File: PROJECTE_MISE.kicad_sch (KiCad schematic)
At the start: 37 parts, among them IC1 MSP430FR2355TPT, J1 conn_DFrobot, J2 ESP01_WiFi_mod, J3 Conn_TX_TP, J4 conn_ACLK_{TP}, J5 conn_SMCLK_{TP}, J6 Conn_RX_TP, J7 conn_SBW, SW1 ~{RST_{MSP}}, U1 LMV324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

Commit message: layout 0 errors 0 warnings
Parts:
- J3, J4, J5, J6: footprint Connector_PinHeader_1.27mm:PinHeader_1x01_P1.27mm_Vertical -> Connector_PinHeader_2.00mm:PinHeader_1x01_P2.00mm_Vertical
- JP1: footprint Connector_PinHeader_1.27mm:PinHeader_2x01_P1.27mm_Vertical -> Connector_PinHeader_2.00mm:PinHeader_2x01_P2.00mm_Vertical
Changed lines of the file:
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@@
 			)
 		)
-		(property "Footprint" "Connector_PinHeader_1.27mm:PinHeader_1x01_P1.27mm_Vertical"
+		(property "Footprint" "Connector_PinHeader_2.00mm:PinHeader_1x01_P2.00mm_Vertical"
 			(at 414.02 223.52 0)
 			(effects
@@
 			)
 		)
-		(property "Footprint" "Connector_PinHeader_1.27mm:PinHeader_1x01_P1.27mm_Vertical"
+		(property "Footprint" "Connector_PinHeader_2.00mm:PinHeader_1x01_P2.00mm_Vertical"
 			(at 132.08 149.86 0)
 			(effects
@@
 			)
 		)
-		(property "Footprint" "Connector_PinHeader_1.27mm:PinHeader_1x01_P1.27mm_Vertical"
+		(property "Footprint" "Connector_PinHeader_2.00mm:PinHeader_1x01_P2.00mm_Vertical"
 			(at 412.75 218.44 0)
 			(effects
@@
 			)
 		)
-		(property "Footprint" "Connector_PinHeader_1.27mm:PinHeader_2x01_P1.27mm_Vertical"
+		(property "Footprint" "Connector_PinHeader_2.00mm:PinHeader_2x01_P2.00mm_Vertical"
 			(at 176.53 354.33 0)
 			(effects
@@
 			)
 		)
-		(property "Footprint" "Connector_PinHeader_1.27mm:PinHeader_1x01_P1.27mm_Vertical"
+		(property "Footprint" "Connector_PinHeader_2.00mm:PinHeader_1x01_P2.00mm_Vertical"
 			(at 132.08 157.48 0)
 			(effects

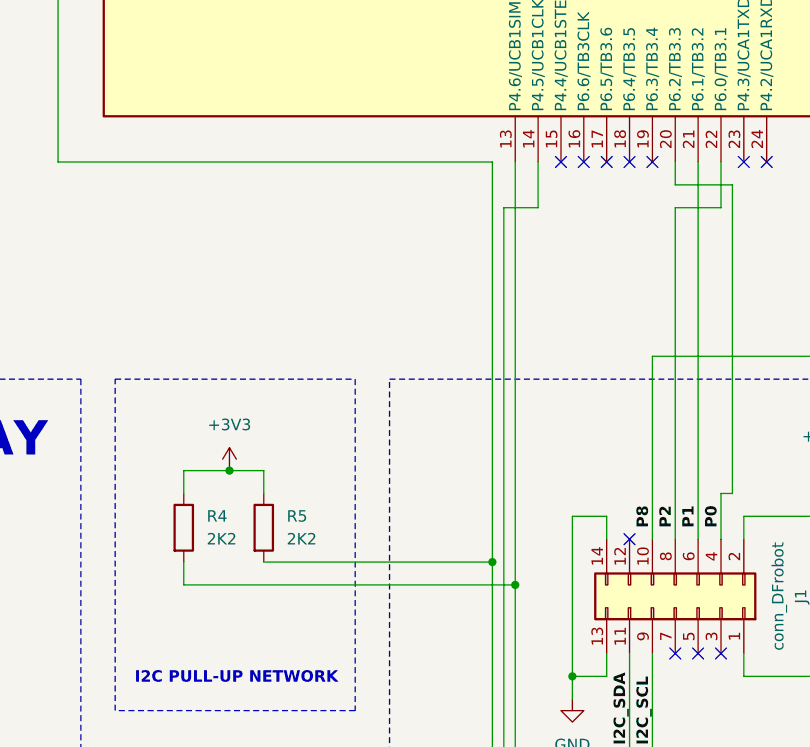
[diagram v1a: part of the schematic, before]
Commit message: layout finished 0 errors, 0 warnings and solved problems
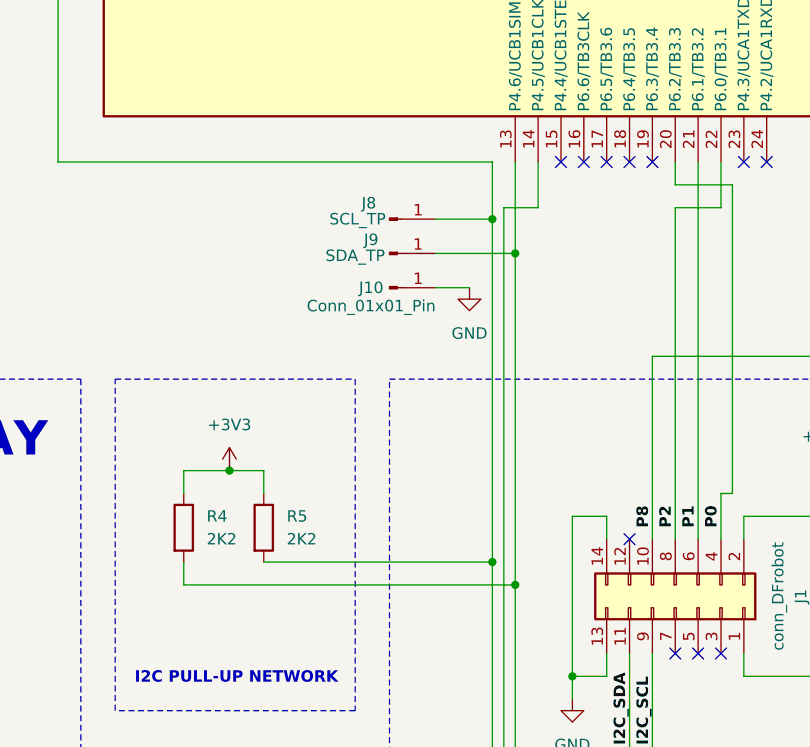
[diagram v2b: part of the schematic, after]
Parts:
- added J10: Conn_01x01_Pin, Connector_PinHeader_2.00mm:PinHeader_1x01_P2.00mm_Vertical, symbol Connector:Conn_01x01_Pin
- added J8: SCL_TP, Connector_PinHeader_2.00mm:PinHeader_1x01_P2.00mm_Vertical, symbol Connector:Conn_01x01_Pin
- added J9: SDA_TP, Connector_PinHeader_2.00mm:PinHeader_1x01_P2.00mm_Vertical, symbol Connector:Conn_01x01_Pin
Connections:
- net GND: now also J10.1 (Pin_1)
- net I2C_SCL: now also J8.1 (Pin_1)
- net I2C_SDA: now also J9.1 (Pin_1)

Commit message: final layout + gerbers
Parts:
- added C7: 100n, Capacitor_SMD:C_0805_2012Metric, symbol Device:C
- R14: value R -> 10K
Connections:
- net +3V3: now also C7.1
- net GND: now also C7.2
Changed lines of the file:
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@@
 	)
 	(junction
+		(at 290.83 113.03)
+		(diameter 0)
+		(color 0 0 0 0)
+	)
+	(junction
 		(at 266.7 350.52)
 		(diameter 0)
@@
 	)
 	(junction
+		(at 290.83 128.27)
+		(diameter 0)
+		(color 0 0 0 0)
+	)
+	(junction
 		(at 190.5 335.28)
 		(diameter 0)
@@
 	(wire
 		(pts
+			(xy 285.75 124.46) (xy 285.75 128.27)
+		)
+		(stroke
+			(width 0)
+			(type default)
+		)
+	)
+	(wire
+		(pts
 			(xy 130.81 187.96) (xy 130.81 189.23)
 		)
@@
 	(wire
 		(pts
+			(xy 285.75 116.84) (xy 285.75 113.03)
+		)
+		(stroke
+			(width 0)
+			(type default)
+		)
+	)
+	(wire
+		(pts
 			(xy 251.46 303.53) (xy 260.35 303.53)
 		)
@@
 	(wire
 		(pts
+			(xy 285.75 113.03) (xy 290.83 113.03)
+		)
+		(stroke
+			(width 0)
+			(type default)
+		)
+	)
+	(wire
+		(pts
 			(xy 367.03 104.14) (xy 367.03 107.95)
 		)
@@
 	(wire
 		(pts
+			(xy 285.75 128.27) (xy 290.83 128.27)
+		)
+		(stroke
+			(width 0)
+			(type default)
+		)
+	)
+	(wire
+		(pts
 			(xy 217.17 105.41) (xy 217.17 110.49)
 		)
@@
 	)
 	(rectangle
-		(start 284.48 77.47)
+		(start 279.4 77.47)
 		(end 431.8 153.67)
 		(stroke
@@
 			)
 		)
-		(property "Value" "R"
+		(property "Value" "10K"
 			(at 364.49 219.7099 0)
 			(effects
@@
 				)
 			)
+		)
+	)
+	(symbol
+		(lib_id "Device:C")
+		(at 285.75 120.65 0)
+		(unit 1)
+		(exclude_from_sim no)
+		(in_bom yes)
+		(on_board yes)
+		(dnp no)
+		(property "Reference" "C7"
+			(at 284.988 123.19 0)
+			(effects
+				(font
+					(size 1.27 1.27)
+				)
+				(justify right)
+			)
+		)
+		(property "Value" "100n"
+			(at 284.988 125.73 0)
+			(effects
+				(font
+					(size 1.27 1.27)
+				)
+				(justify right)
+			)
+		)
+		(property "Footprint" "Capacitor_SMD:C_0805_2012Metric"
+			(at 286.7152 124.46 0)
+			(effects
+				(font
+					(size 1.27 1.27)
+				)
+				(hide yes)
+			)
+		)
+		(property "Datasheet" "~"
+			(at 285.75 120.65 0)
+			(effects
+				(font
+					(size 1.27 1.27)
+				)
+				(hide yes)
+			)
+		)
+		(property "Description" "Unpolarized capacitor"
+			(at 285.75 120.65 0)
+			(effects
+				(font
+					(size 1.27 1.27)
+				)
+				(hide yes)
+			)
+		)
+		(pin "2"
+		)
+		(pin "1"
+		)
+		(instances
+			(project ""
+				(path "/2ce3dfc3-2620-4194-b98c-290dfb7c6429"
+					(reference "C7")
+					(unit 1)
+				)
+			)

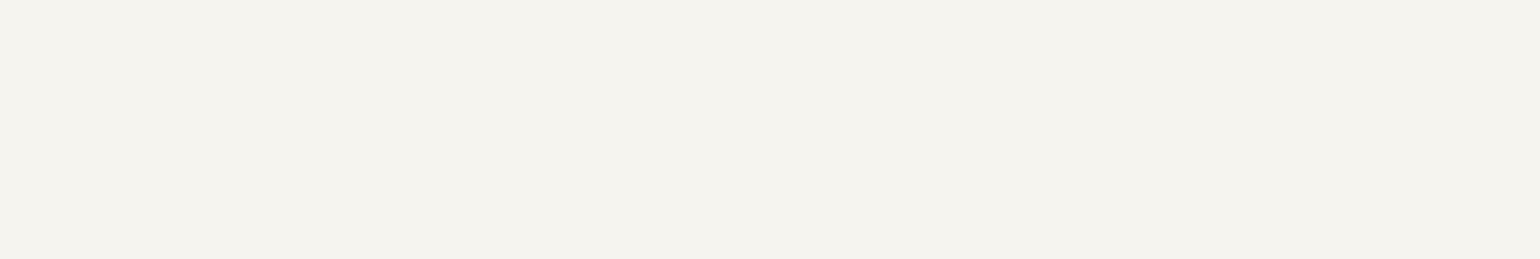
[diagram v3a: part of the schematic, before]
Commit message: fixes layout + pending VCC LED, C ESP & redraw gerbers
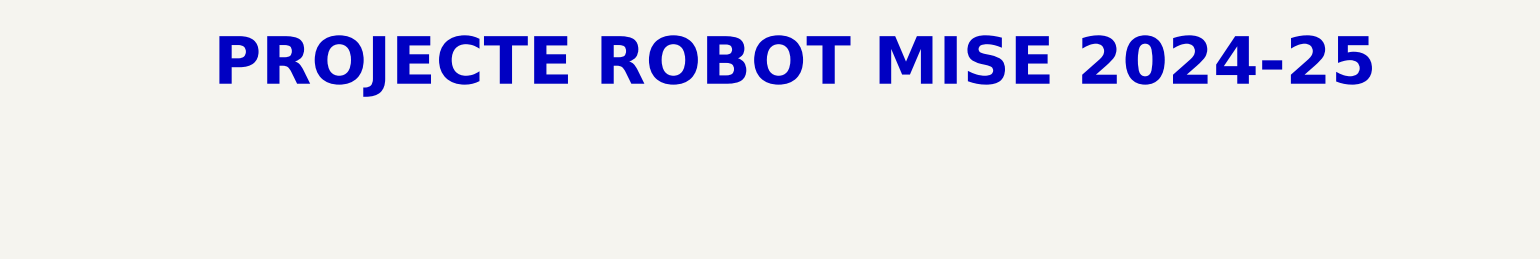
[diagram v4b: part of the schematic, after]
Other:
- note added: "PROJECTE ROBOT MISE 2024-25"
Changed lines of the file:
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@@
 	(title_block
 		(title "Projecte Robot MISE 2024-25")
-		(rev "25/02/25")
+		(date "2025-03-12")
+		(rev "12/03/25")
 		(company "David García - Aidar Iglesias")
 	)
@@
 			)
 		)
+	)
+	(text "PROJECTE ROBOT MISE 2024-25"
+		(exclude_from_sim no)
+		(at 314.452 26.162 0)
+		(effects
+			(font
+				(size 7.62 7.62)
+				(thickness 1.524)
+				(bold yes)
+			)
+		)

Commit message: layout finished
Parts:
- added C8: 100n, Capacitor_SMD:C_0805_2012Metric, symbol Device:C
- added D1: LED, LED_SMD:LED_0805_2012Metric, symbol Device:LED
- added R7: 100, Resistor_SMD:R_0805_2012Metric, symbol Device:R
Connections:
- net +3V3: now also C8.1, D1.2 (A)
- net GND: now also C8.2, R7.2
- new net LED_PS: D1.1 (K), R7.1
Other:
- note added: "LED ALIMENTACIO"

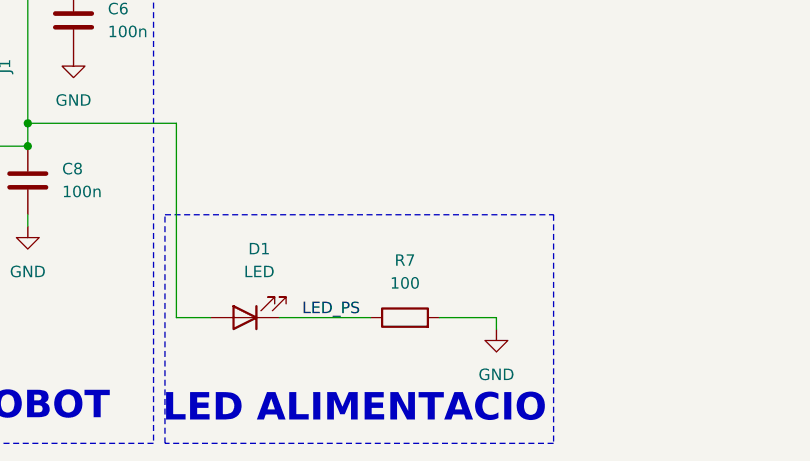
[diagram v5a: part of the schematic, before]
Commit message: update R value LED_PS + update gerber files
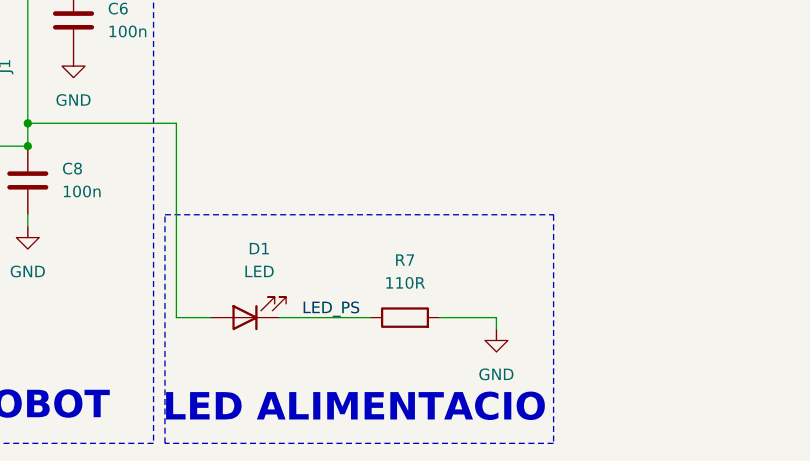
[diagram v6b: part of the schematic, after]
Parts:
- R7: value 100 -> 110R
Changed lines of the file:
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@@
 			)
 		)
-		(property "Value" "100"
+		(property "Value" "110R"
 			(at 336.55 365.76 90)
 			(effects
